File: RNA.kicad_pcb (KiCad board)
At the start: 2 copper layers, 134 x 177 mm, 164 parts, among them J1 USB_B_Micro, J2 SM04B-SRSS-TB(LF)(SN), J3 AudioJack4, J4 Conn_01x06, J5 SM04B-SRSS-TB(LF)(SN), SW1 SW_SPST, SW10 CPG135001S30, SW11 CPG135001S30, SW12 CPG135001S30, SW13 CPG135001S30, SW14 CPG135001S30, SW15 CPG135001S30, SW16 CPG135001S30, SW17 CPG135001S30, SW18 CPG135001S30, SW19 CPG135001S30, SW2 SW_Push, SW20 CPG135001S30, SW21 CPG135001S30, SW22 CPG135001S30, SW23 CPG135001S30, SW24 CPG135001S30, SW25 CPG135001S30, SW26 CPG135001S30, SW27 CPG135001S30, SW28 CPG135001S30, SW29 CPG135001S30, SW3 CPG135001S30, SW30 CPG135001S30, SW31 CPG135001S30, SW32 CPG135001S30, SW33 CPG135001S30, SW34 CPG135001S30, SW35 CPG135001S30, SW36 CPG135001S30, SW37 CPG135001S30, SW38 CPG135001S30, SW39 CPG135001S30, SW4 CPG135001S30, SW40 CPG135001S30, SW41 CPG135001S30, SW42 CPG135001S30, SW43 CPG135001S30, SW44 CPG135001S30, SW45 CPG135001S30, SW46 CPG135001S30, SW47 CPG135001S30, SW48 CPG135001S30, SW49 CPG135001S30, SW5 CPG135001S30, SW50 CPG135001S30, SW51 CPG135001S30, SW52 CPG135001S30, SW53 CPG135001S30, SW54 CPG135001S30, SW55 CPG135001S30, SW56 CPG135001S30, SW57 CPG135001S30, SW58 CPG135001S30, SW59 CPG135001S30, SW6 CPG135001S30, SW60 CPG135001S30, SW61 CPG135001S30, SW62 CPG135001S30, SW63 CPG135001S30, SW64 CPG135001S30, SW65 CPG135001S30, SW66 CPG135001S30, SW7 CPG135001S30, SW8 CPG135001S30, SW9 CPG135001S30, U1 STM32F072C8Tx, U2 PRTR5V0U2X, U3 MCP1703A-3302_SOT23, U4 CAT24M01W, U5 MCP23017_SS

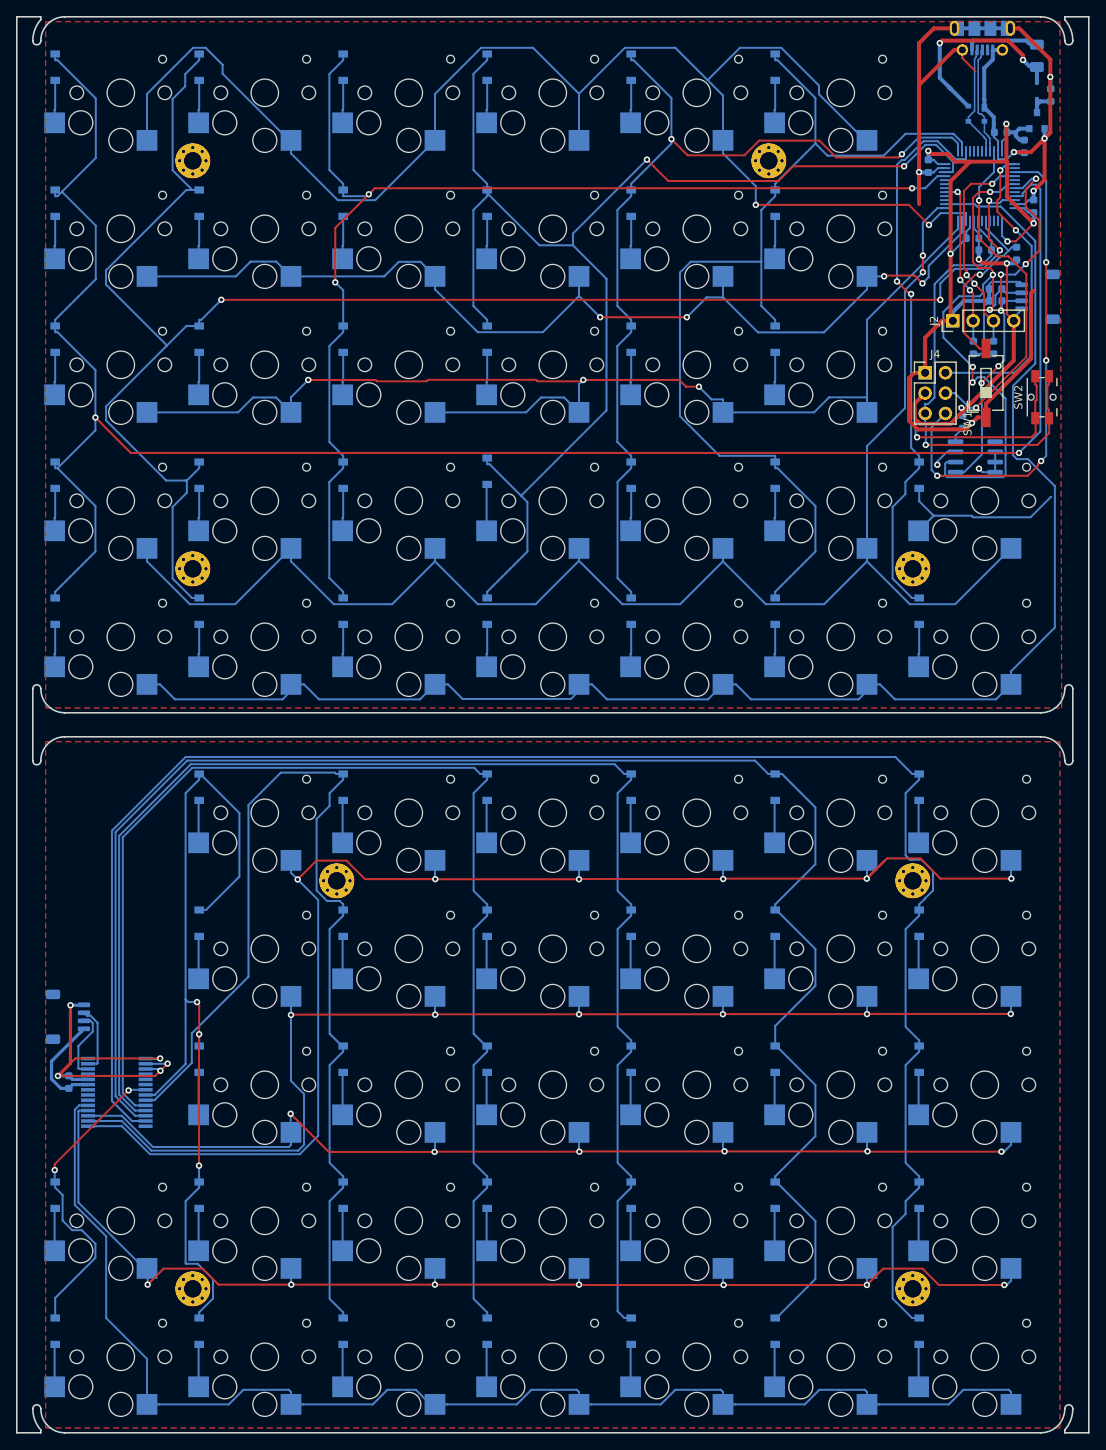
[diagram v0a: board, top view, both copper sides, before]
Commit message: chenge microcontroller from STM32L433CCT to STM32F072BCT
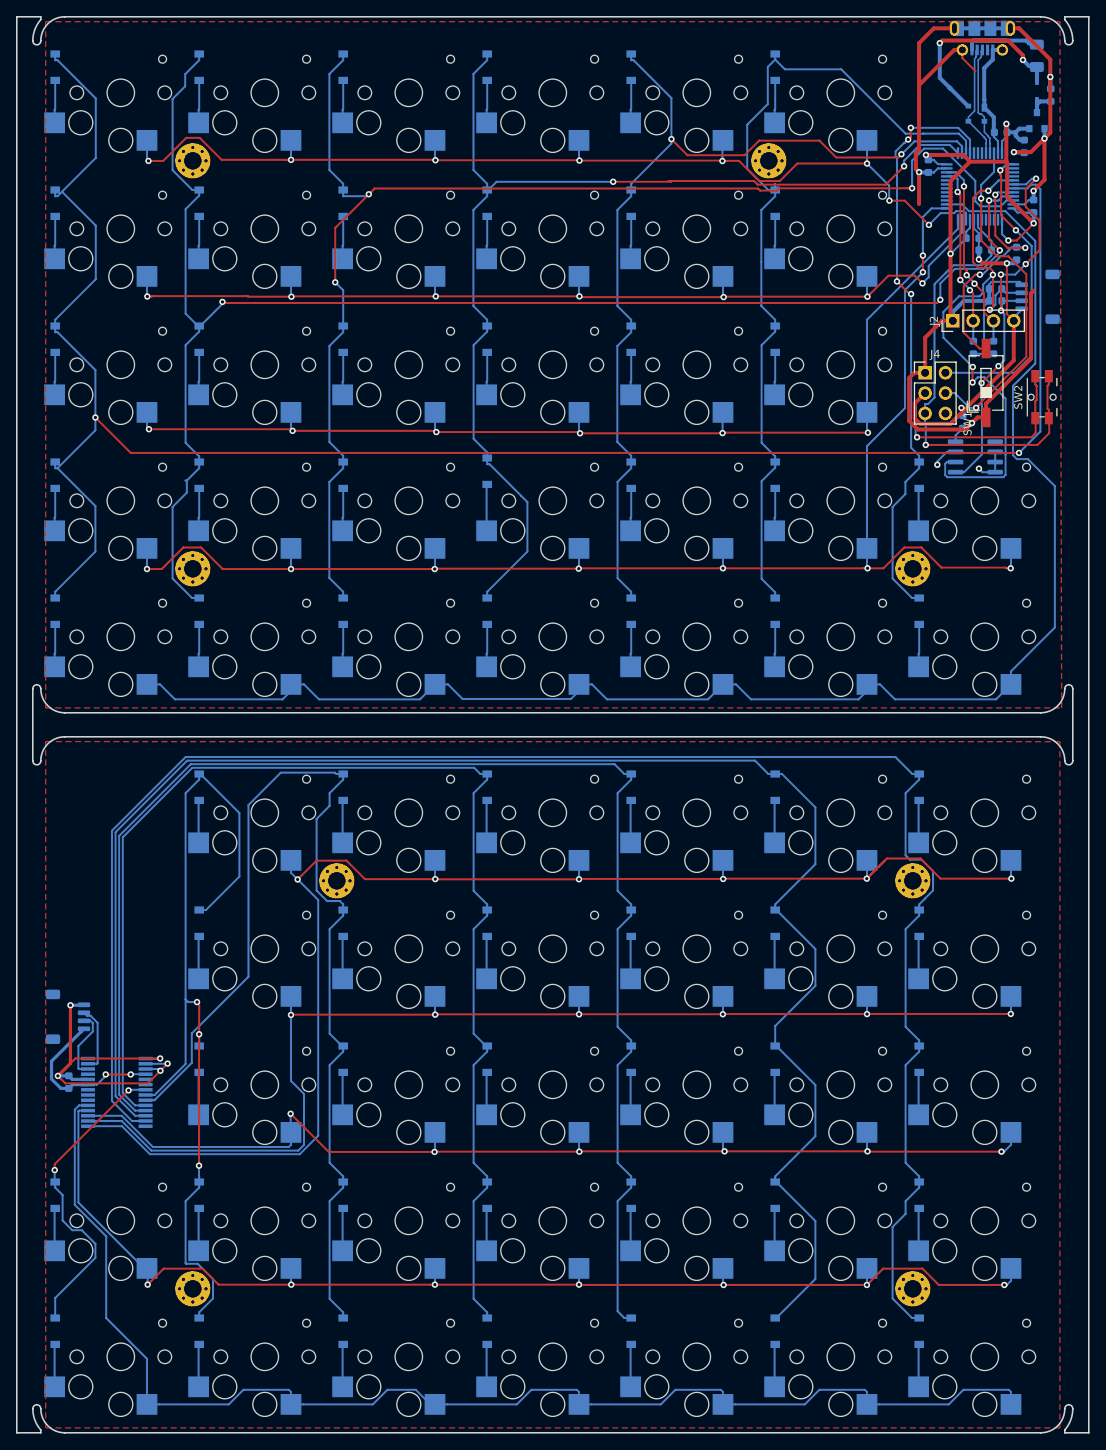
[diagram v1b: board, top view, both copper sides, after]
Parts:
- J2: value SM04B-SRSS-TB(LF)(SN) -> PinHeader_01x04
- J3: value AudioJack4 -> JST SM04B
- U1: value STM32F072C8Tx -> STM32F072CBTx
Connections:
- J2 pad 2: SCL3 -> SCL2
- J2 pad 3: SDA3 -> SDA2
- J4 pad 6: SWO -> Net-(J4-Pad6)
- R2 pad 2: SDA3 -> SDA2
- R3 pad 2: SCL3 -> SCL2
- U1 pad 17: SCL3 -> Net-(U1-Pad17)
- U1 pad 21: COL3 -> SCL2
- U1 pad 22: COL4 -> SDA2
- U1 pad 25: COL5 -> COL4
- U1 pad 26: COL6 -> COL5
- U1 pad 27: COL7 -> COL6
- U1 pad 28: Net-(U1-Pad28) -> COL7
- U1 pad 39: SWO -> Net-(U1-Pad39)
- U1 pad 40: SDA3 -> Net-(U1-Pad40)
- U1 pad 41: Net-(U1-Pad41) -> SCL1
- U1 pad 42: SCL1 -> SDA1
- U1 pad 43: SDA1 -> COL1
- U1 pad 44: Net-(U1-Pad44) -> BOOT0
- U1 pad 45: COL1 -> COL2
- U1 pad 46: COL2 -> COL3
- U1 pad 5: BOOT0 -> Net-(U1-Pad5)
- U5 pad 18: Net-(U5-Pad18) -> VDD
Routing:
- net SWO: track 62.4 -> 0.00 mm, vias 4 -> 0
- net ROW1: track 185.4 -> 128.5 mm, vias 2 -> 8
- net COL4: track 169.2 -> 139.4 mm
- net SDA3: track 27.5 -> 0.00 mm, vias 3 -> 0
- net SDA2: track 0.00 -> 24.3 mm, vias 0 -> 3
- net COL2: track 215.7 -> 193.3 mm
- net SCL2: track 0.00 -> 22.4 mm, vias 0 -> 3
- net SCL3: track 21.0 -> 0.00 mm, vias 3 -> 0
- net COL6: track 126.2 -> 106.1 mm
- net Net-(D32-Pad2): track 22.6 -> 5.33 mm
- net COL3: track 151.0 -> 167.9 mm
- net ROW3: track 150.5 -> 133.7 mm, vias 3 -> 6
- net ROW4: track 192.8 -> 181.1 mm, vias 2 -> 9
- net BOOT0: track 23.0 -> 31.7 mm, vias 1 -> 3
- net VDD: track 158.4 -> 166.7 mm, vias 6 -> 8
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
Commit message: add pull-up resistor for NRST
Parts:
- added C10: 22n, Capacitor_SMD:C_0603_1608Metric, B.Cu at (34.1, 155.6)
- added FL1: EMI_Filter_CommonMode, Filter:ACM2012-121-2P-T002, B.Cu at (136.3, 30.7)
- added R6: 100k, DigiKey:0603, B.Cu at (129.5, 58.4)
- added R7: 10k, Resistor_SMD:R_0603_1608Metric, B.Cu at (32.5, 147.4)
- U2: value PRTR5V0U2X -> USBLC6-2SC6; footprint random-keyboard-parts:SOT143B -> Package_TO_SOT_SMD:SOT-23-6
- U5: value MCP23017_SS -> PCA9555PW; footprint Package_SO:SSOP-28_5.3x10.2mm_P0.65mm -> Package_SO:TSSOP-24_4.4x7.8mm_P0.65mm
- moved C9 10.6 mm to (32.6, 155.6)
- moved U2 4.39 mm to (136.4, 26.7)
- moved U5 1.02 mm to (27.8, 152.8), turned to 180 degrees
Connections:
- J1 pad 2: D- -> Net-(J1-Pad2)
- J1 pad 3: D+ -> Net-(J1-Pad3)
- U2 pad 1: GND -> Net-(J1-Pad2)
- U2 pad 2: D+ -> GND
- U2 pad 3: D- -> Net-(J1-Pad3)
- U2 pad 4: VBUS -> Net-(FL1-Pad3)
- U5 pad 1: ROW1S -> Net-(R7-Pad2)
- U5 pad 10: GND -> COL7S
- U5 pad 12: SCL -> VDD
- U5 pad 13: SDA -> ROW1S
- U5 pad 14: Net-(U5-Pad14) -> ROW2S
- U5 pad 15: GND -> ROW3S
- U5 pad 16: GND -> ROW4S
- U5 pad 17: GND -> ROW5S
- U5 pad 18: VDD -> Net-(U5-Pad18)
- U5 pad 2: ROW2S -> GND
- U5 pad 21: COL1S -> GND
- U5 pad 22: COL2S -> SCL
- U5 pad 23: COL3S -> SDA
- U5 pad 24: COL4S -> GND
- U5 pad 3: ROW3S -> GND
- U5 pad 4: ROW4S -> COL1S
- U5 pad 5: ROW5S -> COL2S
- U5 pad 6: Net-(U5-Pad6) -> COL3S
- U5 pad 7: Net-(U5-Pad7) -> COL4S
- U5 pad 8: Net-(U5-Pad8) -> COL5S
- U5 pad 9: VDD -> COL6S
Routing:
- net GND: track 234.3 -> 196.7 mm
- net VDD: track 166.7 -> 182.4 mm, vias 8 -> 9
- net D-: track 14.1 -> 5.17 mm
- net D+: track 13.6 -> 4.84 mm
- net VBUS: track 25.7 -> 21.9 mm
- net Net-(J1-Pad2): track 0.00 -> 3.09 mm
- net Net-(J1-Pad3): track 0.00 -> 2.98 mm
- net NRST: track 57.8 -> 60.3 mm
- net COL7S: track 222.7 -> 220.3 mm
- net Net-(R7-Pad2): track 0.00 -> 2.26 mm
- net COL6S: track 210.1 -> 208.0 mm
- net Net-(FL1-Pad3): track 0.00 -> 2.14 mm
- net Net-(FL1-Pad1): track 0.00 -> 2.08 mm
- net COL4S: track 158.7 -> 156.7 mm
- net COL5S: track 178.8 -> 176.8 mm
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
